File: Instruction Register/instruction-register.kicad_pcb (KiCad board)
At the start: 2 copper layers, 78.7 x 58.4 mm, 46 parts, among them J1 Bus, J2 Instruction, J3 Misc, J4 Power, U1 74LS245, U2 74LS173, U3 74LS173

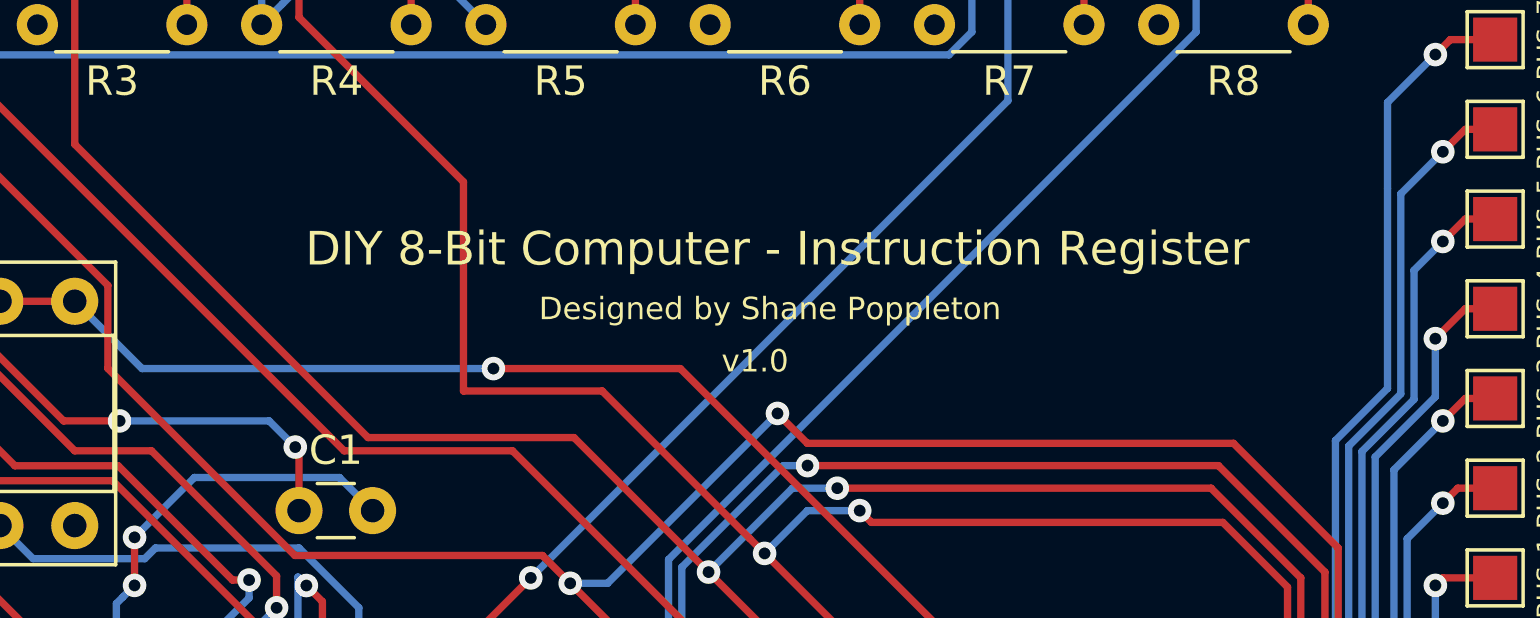
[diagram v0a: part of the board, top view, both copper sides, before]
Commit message: Added Attribution on each PCB, and regenerated gerbers
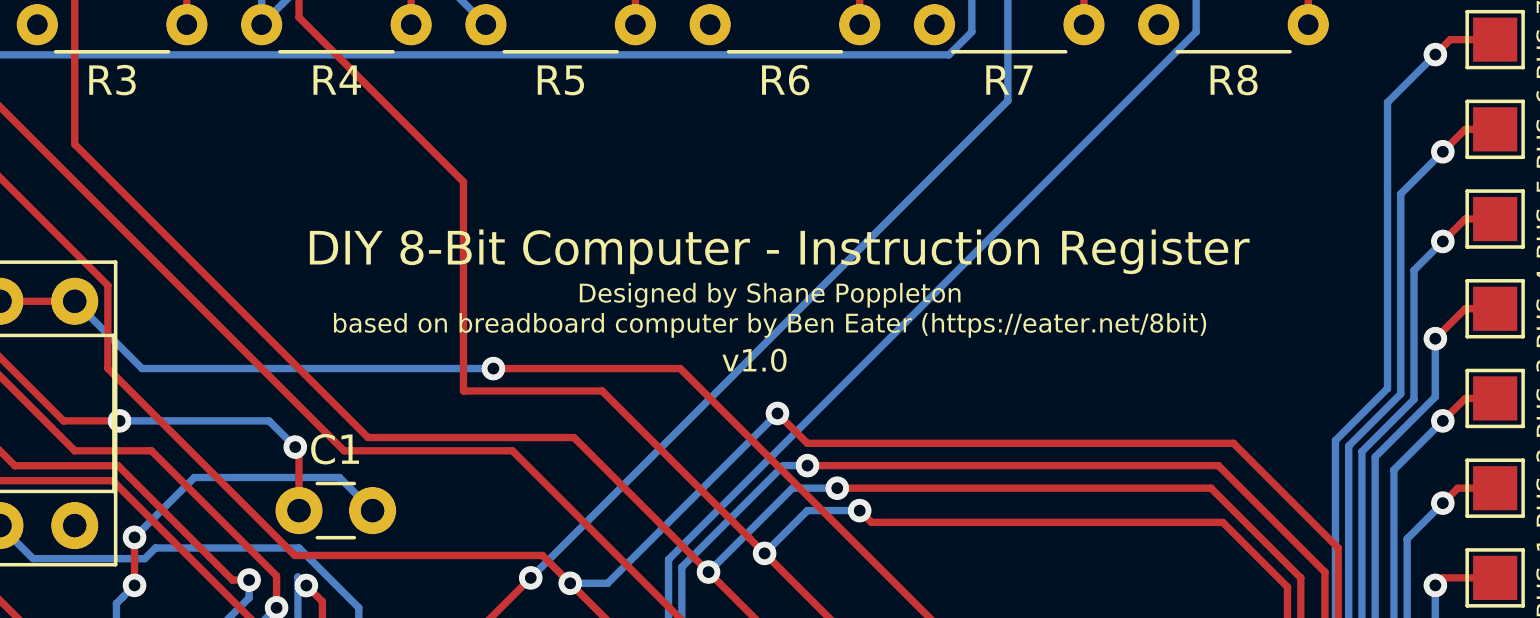
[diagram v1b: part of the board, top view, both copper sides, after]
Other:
- board text added: "Designed by Shane Poppleton based on breadboard computer by Ben Eater (https://eater.net/8bit)"
- board text removed: "Designed by Shane Poppleton"
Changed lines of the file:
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@@
     (effects (font (size 0.762 0.762) (thickness 0.127)))
   )
-  (gr_text "Designed by Shane Poppleton" (at 65.532 66.802) (layer F.SilkS)
-    (effects (font (size 0.762 0.762) (thickness 0.127)))
+  (gr_text "Designed by Shane Poppleton\nbased on breadboard computer by Ben Eater (https://eater.net/8bit)\n" (at 65.532 66.802) (layer F.SilkS)
+    (effects (font (size 0.635 0.635) (thickness 0.1016)))
   )
   (gr_text "DIY 8-Bit Computer - Instruction Register" (at 65.786 64.77) (layer F.SilkS)
